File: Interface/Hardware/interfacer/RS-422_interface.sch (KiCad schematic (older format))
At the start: 26 parts, among them J16 DC/DC in, J17 5V isolated, J18 RJ45, U5 NXJ1S0505MC, U6 ISO7421E, U7 ISO7421E, U8 SN65LBC179A, U9 SN65LBC179A

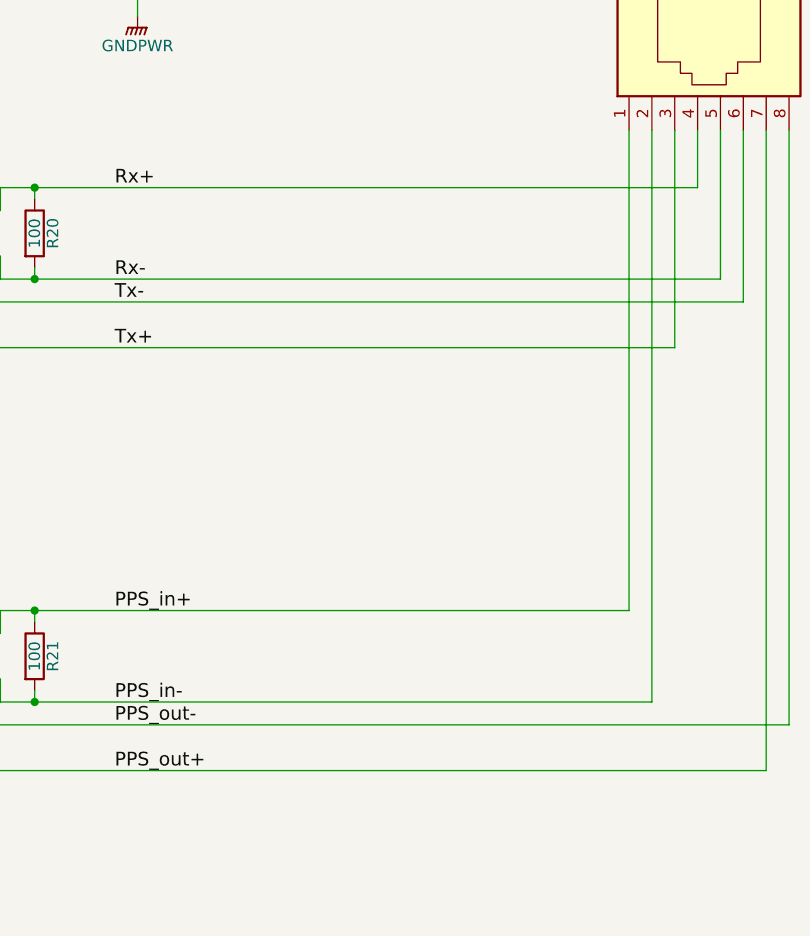
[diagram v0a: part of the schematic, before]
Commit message: line UART out
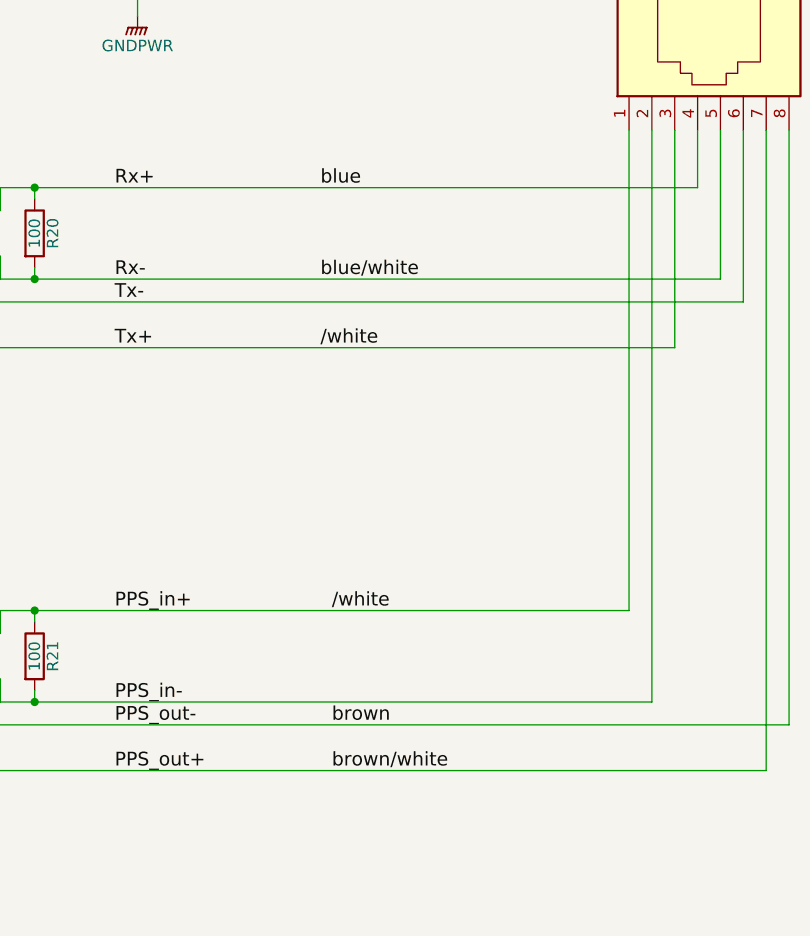
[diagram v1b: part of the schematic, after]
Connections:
- net Tx+ is gone; now on net /white: J18.3, U8.5 (Y)
- net PPS_in+ renamed /white
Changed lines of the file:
@@
 	3700 1200 3700 1300
 Connection ~ 3700 1300
+Text Label 8400 2900 0    60   ~ 0
+blue
+Text Label 8400 3300 0    60   ~ 0
+blue/white
+Text Label 8450 5250 0    60   ~ 0
+brown
+Text Label 8450 5450 0    60   ~ 0
+brown/white
+Text Label 8450 4750 0    60   ~ 0
+/white
+Text Label 8400 3600 0    60   ~ 0
+/white
 $EndSCHEMATC
